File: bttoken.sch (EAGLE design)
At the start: 53 parts, among them IC1 0, Q1 32k, Q2 10G7A-12.5KHZ, T1 MMBT3904, X1 FCI-MICRO-USB

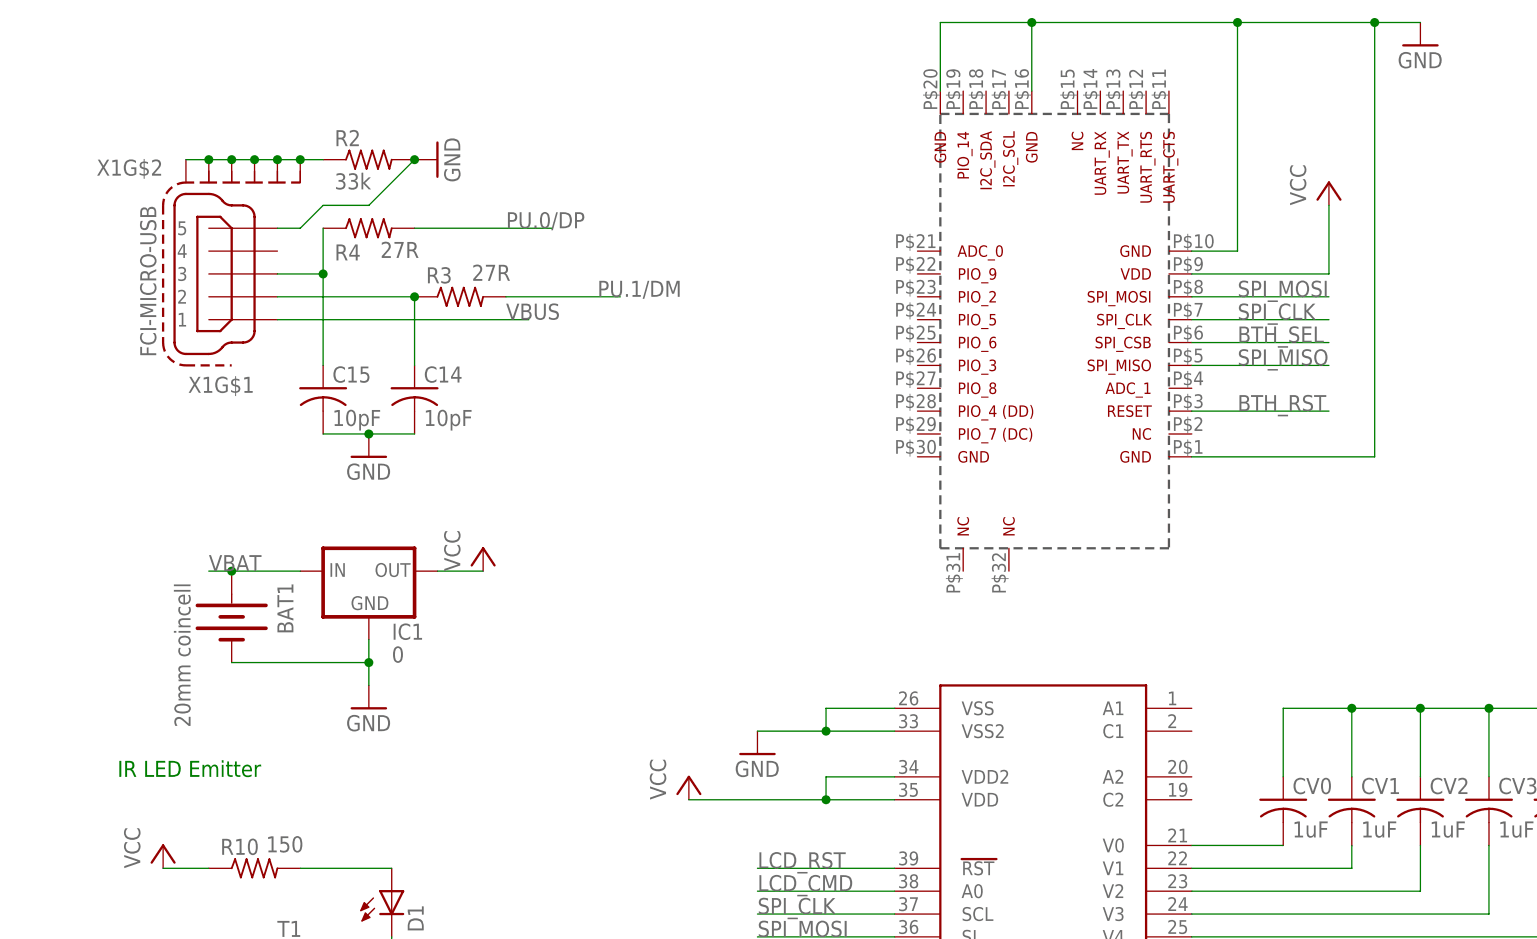
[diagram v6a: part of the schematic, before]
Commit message: New revision with moved quartz, changed filter, etc. Broke autorouting
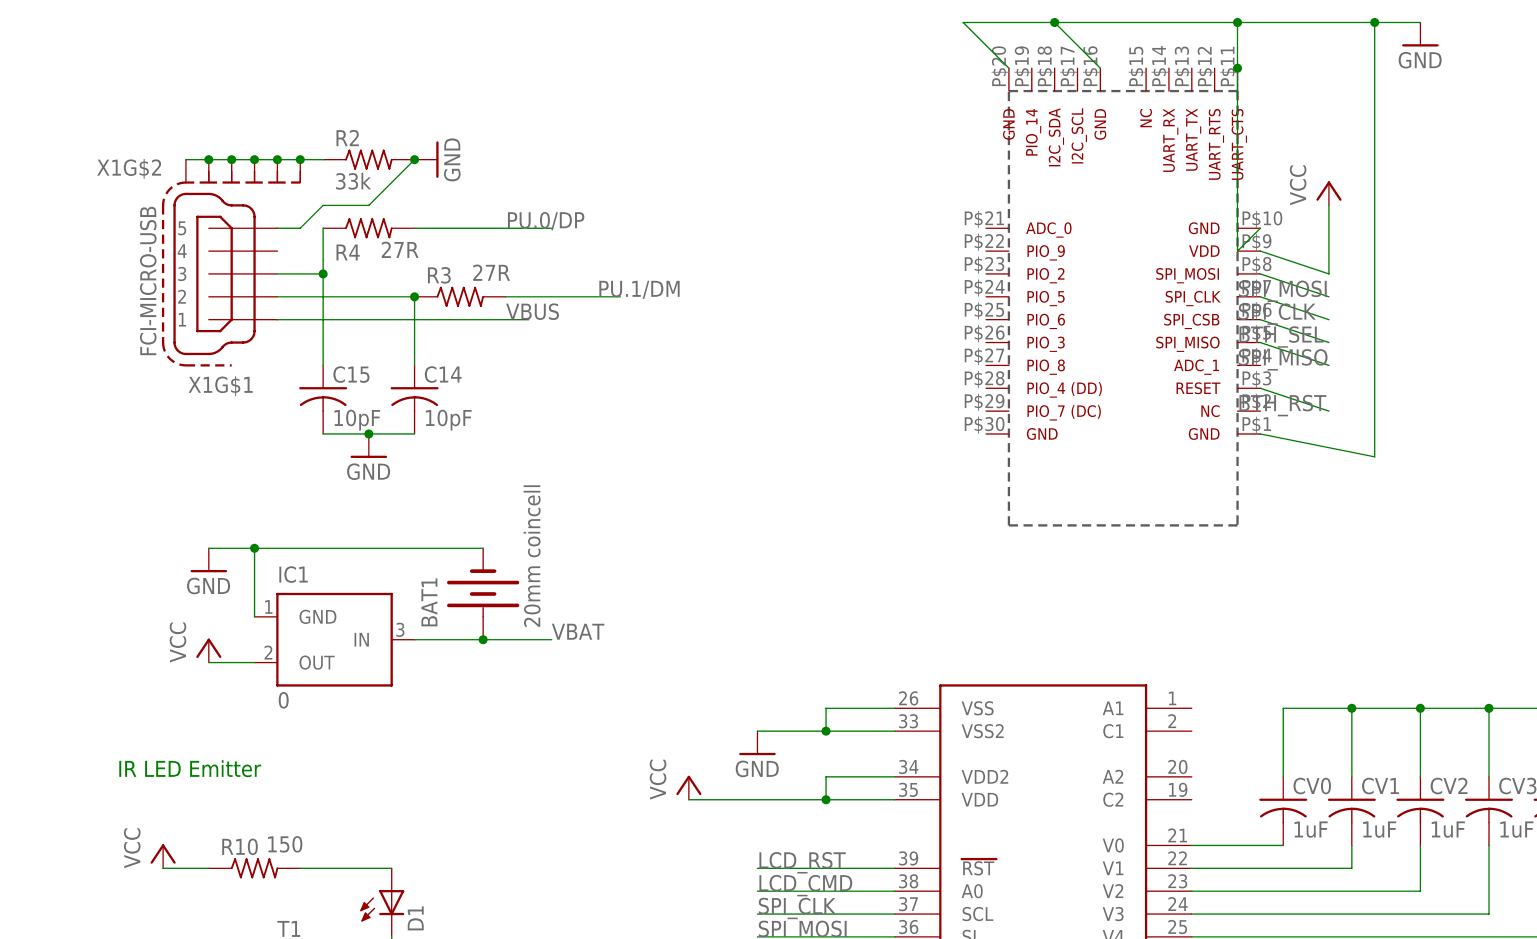
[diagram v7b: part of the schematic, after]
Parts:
- IC1: device adafruit:MCP1700TRI -> DonB:MCP1700
- U$13: value BR-LE4.0-S3 -> BR-LE4.0-S3-NC; device BlueRadios_D2_S2_C46_Eagle_footprint:BR-LE4.0-S3 -> BlueRadios_D2_S2_C46_Eagle_footprint:BR-LE4.0-S3-NC
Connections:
- net GND: now also U$13.P$11
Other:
- moved on the sheet: BAT1
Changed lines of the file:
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@@
 <part name="GND26" library="supply1" deviceset="GND" device=""/>
 <part name="C3P1N" library="rcl" deviceset="C-US" device="C0805" value="1uF"/>
-<part name="U$13" library="BlueRadios_D2_S2_C46_Eagle_footprint" deviceset="BR-LE4.0-S3" device=""/>
+<part name="U$13" library="BlueRadios_D2_S2_C46_Eagle_footprint" deviceset="BR-LE4.0-S3-NC" device=""/>
 <part name="S1" library="SparkFun-Electromechanical" deviceset="SWITCH-MOMENTARY-2" device="-SMD-1101NE" value="SWITCH-MOMENTARY-2-SMD-1101NE"/>
 <part name="GND19" library="supply1" deviceset="GND" device=""/>
@@
 <part name="GND21" library="supply1" deviceset="GND" device=""/>
 <part name="GND17" library="supply1" deviceset="GND" device=""/>
-<part name="IC1" library="adafruit" deviceset="MCP1700" device="TRI" value="0"/>
+<part name="IC1" library="DonB" deviceset="MCP1700" device="" value="0"/>
 <part name="GND22" library="supply1" deviceset="GND" device=""/>
 <part name="P+4" library="supply1" deviceset="VCC" device=""/>
@@
 <instance part="GND26" gate="1" x="149.86" y="200.66"/>
 <instance part="C3P1N" gate="G$1" x="144.78" y="167.64"/>
-<instance part="U$13" gate="G$1" x="78.74" y="233.68" rot="R90"/>
+<instance part="U$13" gate="G$1" x="88.9" y="246.38" rot="R90"/>
 <instance part="S1" gate="G$1" x="48.26" y="114.3" rot="R90"/>
 <instance part="GND19" gate="1" x="48.26" y="121.92" rot="R180"/>
@@
 <instance part="GND21" gate="1" x="7.62" y="160.02"/>
 <instance part="GND17" gate="1" x="121.92" y="276.86"/>
-<instance part="IC1" gate="1" x="5.08" y="218.44"/>
-<instance part="GND22" gate="1" x="5.08" y="203.2"/>
+<instance part="IC1" gate="G$1" x="10.16" y="210.82"/>
+<instance part="GND22" gate="1" x="-12.7" y="218.44"/>
 <instance part="P+4" gate="VCC" x="40.64" y="48.26"/>
-<instance part="P+5" gate="VCC" x="17.78" y="220.98"/>
+<instance part="P+5" gate="VCC" x="-12.7" y="210.82"/>
 <instance part="P+6" gate="VCC" x="40.64" y="195.58"/>
 <instance part="P+7" gate="VCC" x="111.76" y="261.62"/>
@@
 <instance part="R12" gate="G$1" x="-33.02" y="43.18" rot="R90"/>
 <instance part="LED_CHRG" gate="A" x="-22.86" y="55.88"/>
-<instance part="BAT1" gate="G$1" x="-10.16" y="213.36" rot="R270"/>
+<instance part="BAT1" gate="G$1" x="17.78" y="215.9" rot="R90"/>
 </instances>
 <busses>
@@
 <pinref part="GND17" gate="1" pin="GND"/>
 <wire x1="121.92" y1="279.4" x2="116.84" y2="279.4" width="0.1524" layer="91"/>
-<wire x1="96.52" y1="254" x2="101.6" y2="254" width="0.1524" layer="91"/>
-<wire x1="101.6" y1="254" x2="101.6" y2="279.4" width="0.1524" layer="91"/>
-<wire x1="101.6" y1="279.4" x2="78.74" y2="279.4" width="0.1524" layer="91"/>
-<wire x1="78.74" y1="279.4" x2="78.74" y2="271.78" width="0.1524" layer="91"/>
-<wire x1="68.58" y1="271.78" x2="68.58" y2="279.4" width="0.1524" layer="91"/>
-<wire x1="68.58" y1="279.4" x2="78.74" y2="279.4" width="0.1524" layer="91"/>
-<wire x1="96.52" y1="231.14" x2="116.84" y2="231.14" width="0.1524" layer="91"/>
+<wire x1="104.14" y1="256.54" x2="101.6" y2="254" width="0.1524" layer="91"/>
+<wire x1="101.6" y1="254" x2="101.6" y2="274.32" width="0.1524" layer="91"/>
+<wire x1="101.6" y1="274.32" x2="101.6" y2="279.4" width="0.1524" layer="91"/>
+<wire x1="101.6" y1="279.4" x2="81.28" y2="279.4" width="0.1524" layer="91"/>
+<wire x1="81.28" y1="279.4" x2="86.36" y2="274.32" width="0.1524" layer="91"/>
+<wire x1="76.2" y1="274.32" x2="71.12" y2="279.4" width="0.1524" layer="91"/>
+<wire x1="71.12" y1="279.4" x2="81.28" y2="279.4" width="0.1524" layer="91"/>
+<wire x1="104.14" y1="233.68" x2="116.84" y2="231.14" width="0.1524" layer="91"/>
 <wire x1="116.84" y1="231.14" x2="116.84" y2="279.4" width="0.1524" layer="91"/>
 <wire x1="116.84" y1="279.4" x2="101.6" y2="279.4" width="0.1524" layer="91"/>
-<junction x="78.74" y="279.4"/>
+<junction x="81.28" y="279.4"/>
 <junction x="101.6" y="279.4"/>
 <pinref part="U$13" gate="G$1" pin="P$10"/>
@@
 <pinref part="U$13" gate="G$1" pin="P$1"/>
 <junction x="116.84" y="279.4"/>
+<pinref part="U$13" gate="G$1" pin="P$11"/>
+<junction x="101.6" y="274.32"/>
 </segment>
 <segment>
@@
 </segment>
 <segment>
-<pinref part="IC1" gate="1" pin="GND"/>
+<pinref part="IC1" gate="G$1" pin="GND"/>
 <pinref part="GND22" gate="1" pin="GND"/>
-<wire x1="5.08" y1="205.74" x2="5.08" y2="208.28" width="0.1524" layer="91"/>
+<wire x1="-12.7" y1="220.98" x2="-7.62" y2="220.98" width="0.1524" layer="91"/>
 <pinref part="BAT1" gate="G$1" pin="-"/>
-<wire x1="5.08" y1="208.28" x2="5.08" y2="210.82" width="0.1524" layer="91"/>
-<wire x1="-10.16" y1="208.28" x2="5.08" y2="208.28" width="0.1524" layer="91"/>
-<junction x="5.08" y="208.28"/>
+<wire x1="-7.62" y1="220.98" x2="-7.62" y2="213.36" width="0.1524" layer="91"/>
+<wire x1="17.78" y1="220.98" x2="-7.62" y2="220.98" width="0.1524" layer="91"/>
+<junction x="-7.62" y="220.98"/>
 </segment>
 <segment>
@@
 </segment>
 <segment>
-<wire x1="96.52" y1="248.92" x2="111.76" y2="248.92" width="0.1524" layer="91"/>
+<wire x1="104.14" y1="251.46" x2="111.76" y2="248.92" width="0.1524" layer="91"/>
 <label x="101.6" y="248.92" size="1.778" layer="95"/>
 <pinref part="U$13" gate="G$1" pin="P$8"/>
@@
 <net name="BTH_SEL" class="0">
 <segment>
-<wire x1="96.52" y1="243.84" x2="111.76" y2="243.84" width="0.1524" layer="91"/>
+<wire x1="104.14" y1="246.38" x2="111.76" y2="243.84" width="0.1524" layer="91"/>
 <label x="101.6" y="243.84" size="1.778" layer="95"/>
 <pinref part="U$13" gate="G$1" pin="P$6"/>
@@
 <net name="SPI_MISO" class="0">
 <segment>
-<wire x1="96.52" y1="241.3" x2="111.76" y2="241.3" width="0.1524" layer="91"/>
+<wire x1="104.14" y1="243.84" x2="111.76" y2="241.3" width="0.1524" layer="91"/>
 <label x="101.6" y="241.3" size="1.778" layer="95"/>
 <pinref part="U$13" gate="G$1" pin="P$5"/>
@@
 <net name="BTH_RST" class="0">
 <segment>
-<wire x1="96.52" y1="236.22" x2="111.76" y2="236.22" width="0.1524" layer="91"/>
+<wire x1="104.14" y1="238.76" x2="111.76" y2="236.22" width="0.1524" layer="91"/>
 <label x="101.6" y="236.22" size="1.778" layer="95"/>
 <pinref part="U$13" gate="G$1" pin="P$3"/>
@@
 </segment>
 <segment>
-<wire x1="96.52" y1="246.38" x2="111.76" y2="246.38" width="0.1524" layer="91"/>
+<wire x1="104.14" y1="248.92" x2="111.76" y2="246.38" width="0.1524" layer="91"/>
 <label x="101.6" y="246.38" size="1.778" layer="95"/>
 <pinref part="U$13" gate="G$1" pin="P$7"/>
@@
 <net name="VBAT" class="0">
 <segment>
-<pinref part="IC1" gate="1" pin="IN"/>
-<wire x1="-2.54" y1="218.44" x2="-10.16" y2="218.44" width="0.1524" layer="91"/>
-<label x="-12.7" y="218.44" size="1.778" layer="95"/>
+<pinref part="IC1" gate="G$1" pin="IN"/>
+<wire x1="10.16" y1="210.82" x2="17.78" y2="210.82" width="0.1524" layer="91"/>
+<label x="25.4" y="210.82" size="1.778" layer="95"/>
 <pinref part="BAT1" gate="G$1" pin="+"/>
-<wire x1="-10.16" y1="218.44" x2="-12.7" y2="218.44" width="0.1524" layer="91"/>
-<junction x="-10.16" y="218.44"/>
+<wire x1="17.78" y1="210.82" x2="25.4" y2="210.82" width="0.1524" layer="91"/>
+<junction x="17.78" y="210.82"/>
 </segment>
 <segment>
@@
 </segment>
 <segment>
-<pinref part="IC1" gate="1" pin="OUT"/>
-<wire x1="17.78" y1="218.44" x2="12.7" y2="218.44" width="0.1524" layer="91"/>
+<pinref part="IC1" gate="G$1" pin="OUT"/>
+<wire x1="-12.7" y1="208.28" x2="-7.62" y2="208.28" width="0.1524" layer="91"/>
 <pinref part="P+5" gate="VCC" pin="VCC"/>
 </segment>
 <segment>
 <pinref part="U$13" gate="G$1" pin="P$9"/>
-<wire x1="96.52" y1="251.46" x2="111.76" y2="251.46" width="0.1524" layer="91"/>
+<wire x1="104.14" y1="254" x2="111.76" y2="251.46" width="0.1524" layer="91"/>
 <pinref part="P+7" gate="VCC" pin="VCC"/>
 <wire x1="111.76" y1="251.46" x2="111.76" y2="259.08" width="0.1524" layer="91"/>
